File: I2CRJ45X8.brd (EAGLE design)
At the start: 80 x 50 mm, 59 parts, among them IC1 MCP23017SO, IC2 MCP23017SO, J1 M02X3-SHROUDED, J2 INT2A, J3 M02X3-PIN, J4 M02X3-PIN, J5 RJ45-X8, J6 M02X3-SHROUDED, J7 INT1A

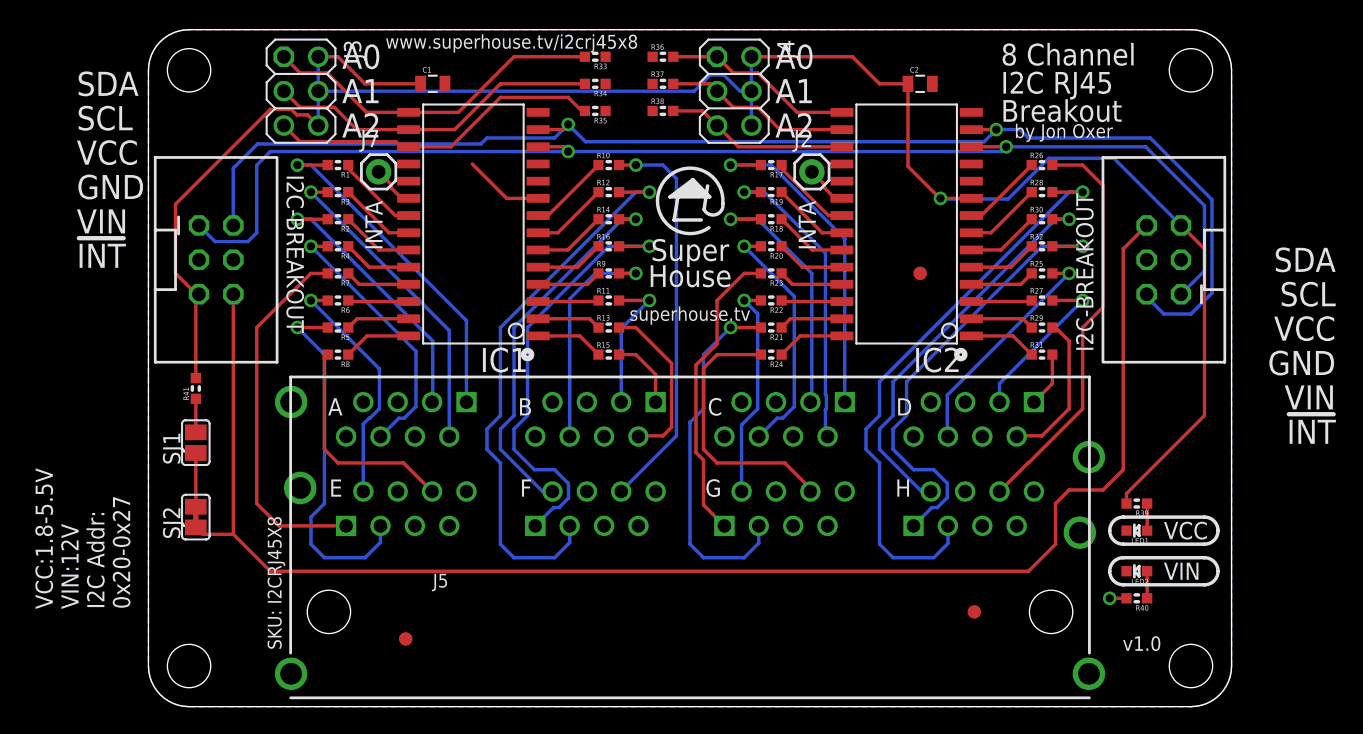
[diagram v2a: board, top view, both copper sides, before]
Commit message: Routing for 2x3 I2C Breakout header
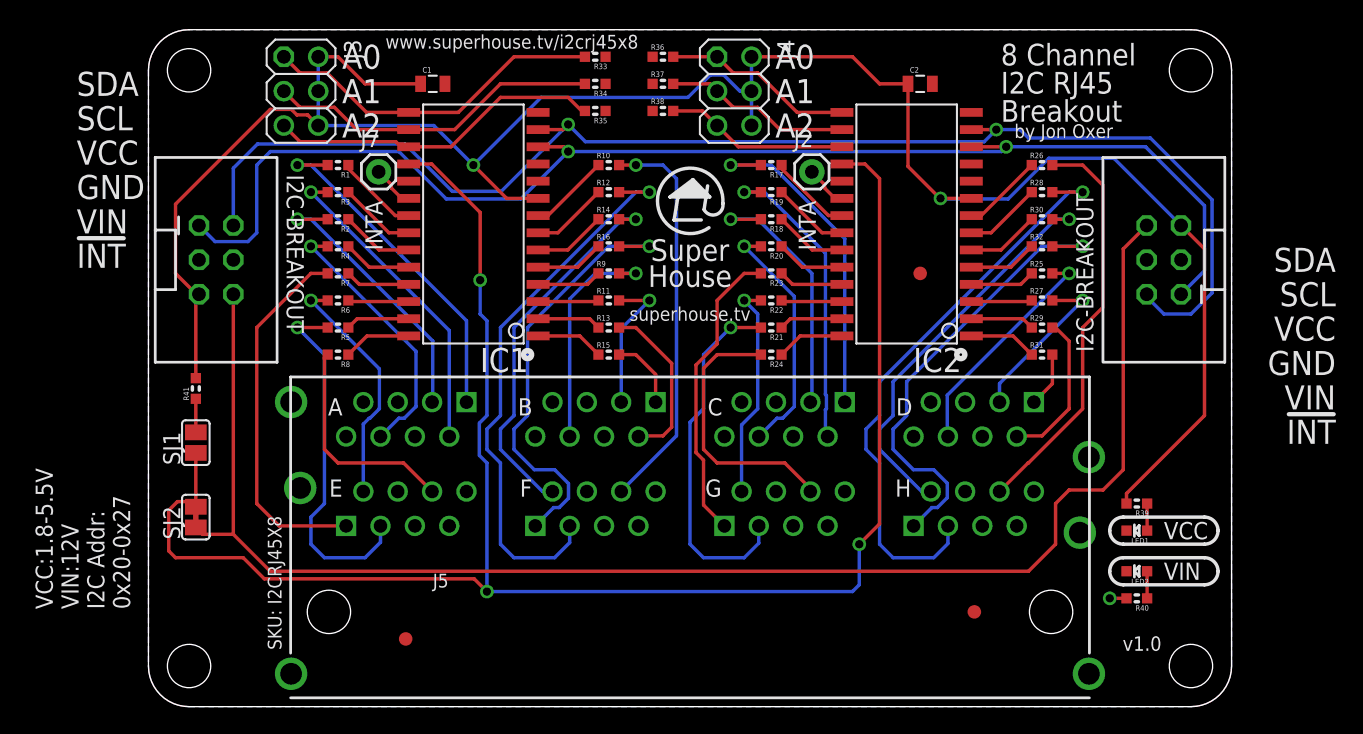
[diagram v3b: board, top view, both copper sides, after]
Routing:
- net !RST: track 3.98 -> 131.0 mm, vias 0 -> 3
- net VCC: track 154.3 -> 157.7 mm, vias 1 -> 2
- net SDA: track 98.2 -> 101.1 mm
- net SCL: track 94.6 -> 97.5 mm
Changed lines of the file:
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@@
 <wire x1="77" y1="29" x2="78.5588" y2="30.5588" width="0.254" layer="16"/>
 <wire x1="78.5588" y1="30.5588" x2="78.5588" y2="37.4412" width="0.254" layer="16"/>
-<wire x1="31" y1="43" x2="30" y2="42" width="0.254" layer="16"/>
-<wire x1="30" y1="42" x2="25" y2="42" width="0.254" layer="16"/>
-<wire x1="25" y1="42" x2="24.5588" y2="41.5588" width="0.254" layer="16"/>
 <wire x1="6.27" y1="39.77" x2="6.27" y2="35.54" width="0.254" layer="16"/>
-<wire x1="24.5588" y1="41.5588" x2="8.0588" y2="41.5588" width="0.254" layer="16"/>
-<wire x1="8.0588" y1="41.5588" x2="6.27" y2="39.77" width="0.254" layer="16"/>
+<wire x1="6.27" y1="39.77" x2="8.0588" y2="41.5588" width="0.254" layer="16"/>
+<wire x1="8.0588" y1="41.5588" x2="18.9412" y2="41.5588" width="0.254" layer="16"/>
+<wire x1="18.9412" y1="41.5588" x2="22.4412" y2="38.0588" width="0.254" layer="16"/>
+<wire x1="22.4412" y1="38.0588" x2="26.0588" y2="38.0588" width="0.254" layer="16"/>
+<wire x1="26.0588" y1="38.0588" x2="31" y2="43" width="0.254" layer="16"/>
 </signal>
 <signal name="SCL">
@@
 <wire x1="78" y1="32.19" x2="76.27" y2="30.46" width="0.254" layer="16"/>
 <wire x1="9" y1="41" x2="8" y2="40" width="0.254" layer="16"/>
-<wire x1="31" y1="41" x2="9" y2="41" width="0.254" layer="16"/>
 <wire x1="7.3462" y1="34.3462" x2="4.9238" y2="34.3462" width="0.254" layer="16"/>
 <wire x1="4.9238" y1="34.3462" x2="3.73" y2="35.54" width="0.254" layer="16"/>
 <wire x1="8" y1="40" x2="8" y2="35" width="0.254" layer="16"/>
 <wire x1="8" y1="35" x2="7.3462" y2="34.3462" width="0.254" layer="16"/>
+<wire x1="31" y1="41" x2="27.5" y2="37.5" width="0.254" layer="16"/>
+<wire x1="22" y1="37.5" x2="19.5" y2="40" width="0.254" layer="16"/>
+<wire x1="19.5" y1="40" x2="18.5" y2="41" width="0.254" layer="16"/>
+<wire x1="18.5" y1="41" x2="9" y2="41" width="0.254" layer="16"/>
+<wire x1="27.5" y1="37.5" x2="22" y2="37.5" width="0.254" layer="16"/>
 </signal>
 <signal name="E1">
@@
 <wire x1="58.5" y1="37.54" x2="60.78" y2="37.54" width="0.254" layer="1"/>
 <contactref element="C1" pad="1"/>
-<wire x1="23.92" y1="40.08" x2="26.46" y2="37.54" width="0.254" layer="1"/>
+<wire x1="26.46" y1="37.54" x2="24" y2="40" width="0.254" layer="1"/>
 <contactref element="C2" pad="1"/>
 <contactref element="J4" pad="6"/>
@@
 <wire x1="16" y1="46" x2="14" y2="48" width="0.254" layer="1"/>
 <wire x1="44" y1="45.46" x2="44.54" y2="46" width="0.254" layer="16"/>
-<wire x1="41.50550625" y1="46.6538" x2="42.49449375" y2="46.6538" width="0.254" layer="16"/>
-<wire x1="12.54" y1="45.46" x2="40.31170625" y2="45.46" width="0.254" layer="16"/>
+<wire x1="42.49449375" y1="46.6538" x2="41.50550625" y2="46.6538" width="0.254" layer="16"/>
 <wire x1="43.68829375" y1="45.46" x2="44" y2="45.46" width="0.254" layer="16"/>
-<wire x1="40.31170625" y1="45.46" x2="41.50550625" y2="46.6538" width="0.254" layer="16"/>
 <wire x1="42.49449375" y1="46.6538" x2="43.68829375" y2="45.46" width="0.254" layer="16"/>
 <wire x1="10.96233125" y1="43.7074" x2="11.7526" y2="43.7074" width="0.254" layer="1"/>
@@
 <wire x1="3.5" y1="24.262" x2="3.5" y2="30.23" width="0.254" layer="1"/>
 <wire x1="3.5" y1="30.23" x2="3.73" y2="30.46" width="0.254" layer="1"/>
-<wire x1="20.1" y1="46" x2="23.92" y2="40.08" width="0" layer="19" extent="1-1"/>
+<wire x1="23.92" y1="40.08" x2="24" y2="40" width="0.254" layer="1"/>
+<via x="24" y="40" extent="1-16" drill="0.6096"/>
+<wire x1="12.54" y1="42.92" x2="21.08" y2="42.92" width="0.254" layer="16"/>
+<wire x1="21.08" y1="42.92" x2="24" y2="40" width="0.254" layer="16"/>
+<wire x1="29" y1="45" x2="24" y2="40" width="0.254" layer="16"/>
+<wire x1="41.50550625" y1="46.6538" x2="39.85170625" y2="45" width="0.254" layer="16"/>
+<wire x1="39.85170625" y1="45" x2="29" y2="45" width="0.254" layer="16"/>
 </signal>
 <signal name="N$2">
@@
 <contactref element="IC1" pad="18"/>
 <contactref element="IC2" pad="18"/>
-<wire x1="3.5" y1="18.738" x2="3.5" y2="14.762" width="0.254" layer="1"/>
-<wire x1="19.22" y1="40.08" x2="51.22" y2="40.08" width="0" layer="19" extent="1-1"/>
-<wire x1="3.5" y1="18.738" x2="19.22" y2="40.08" width="0" layer="19" extent="1-1"/>
+<wire x1="3.5" y1="18.738" x2="3.5" y2="15.143" width="0.254" layer="1"/>
+<wire x1="3.5" y1="15.143" x2="3.5" y2="14.762" width="0.254" layer="1"/>
+<wire x1="19.22" y1="40.08" x2="20.92" y2="40.08" width="0.254" layer="1"/>
+<wire x1="24.5" y1="36.5" x2="24.5" y2="31.5" width="0.254" layer="1"/>
+<via x="24.5" y="31.5" extent="1-16" drill="0.6096"/>
+<wire x1="24.5" y1="29" x2="25" y2="28.5" width="0.254" layer="16"/>
+<wire x1="25" y1="28.5" x2="25" y2="21.5" width="0.254" layer="16"/>
+<wire x1="24.4412" y1="18.5588" x2="25" y2="18" width="0.254" layer="16"/>
+<via x="25" y="8.5" extent="1-16" drill="0.6096"/>
+<wire x1="25" y1="8.5" x2="24.0588" y2="9.4412" width="0.254" layer="1"/>
+<wire x1="2" y1="11" x2="1.5" y2="11.5" width="0.254" layer="1"/>
+<wire x1="1.5" y1="11.5" x2="1.5" y2="14.5" width="0.254" layer="1"/>
+<wire x1="1.5" y1="14.5" x2="2.143" y2="15.143" width="0.254" layer="1"/>
+<wire x1="2.143" y1="15.143" x2="3.5" y2="15.143" width="0.254" layer="1"/>
+<wire x1="20.92" y1="40.08" x2="24.5" y2="36.5" width="0.254" layer="1"/>
+<wire x1="24.5" y1="31.5" x2="24.5" y2="29" width="0.254" layer="16"/>
+<wire x1="25" y1="21.5" x2="24.4412" y2="20.9412" width="0.254" layer="16"/>
+<wire x1="24.4412" y1="20.9412" x2="24.4412" y2="18.5588" width="0.254" layer="16"/>
+<wire x1="25" y1="18" x2="25" y2="8.5" width="0.254" layer="16"/>
+<wire x1="24.0588" y1="9.4412" x2="8.5588" y2="9.4412" width="0.254" layer="1"/>
+<wire x1="8.5588" y1="9.4412" x2="7" y2="11" width="0.254" layer="1"/>
+<wire x1="7" y1="11" x2="2" y2="11" width="0.254" layer="1"/>
+<wire x1="51.22" y1="40.08" x2="52.92" y2="40.08" width="0.254" layer="1"/>
+<wire x1="52.92" y1="40.08" x2="54" y2="39" width="0.254" layer="1"/>
+<wire x1="54" y1="39" x2="54" y2="13.5" width="0.254" layer="1"/>
+<via x="52.5" y="12" extent="1-16" drill="0.6096"/>
+<wire x1="52.5" y1="12" x2="52.5" y2="9" width="0.254" layer="16"/>
+<wire x1="52.5" y1="9" x2="52" y2="8.5" width="0.254" layer="16"/>
+<wire x1="52" y1="8.5" x2="25" y2="8.5" width="0.254" layer="16"/>
+<wire x1="54" y1="13.5" x2="52.5" y2="12" width="0.254" layer="1"/>
 </signal>
 <signal name="N$14">

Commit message: Converted to I2C-BREAKOUT header for v2.0 release
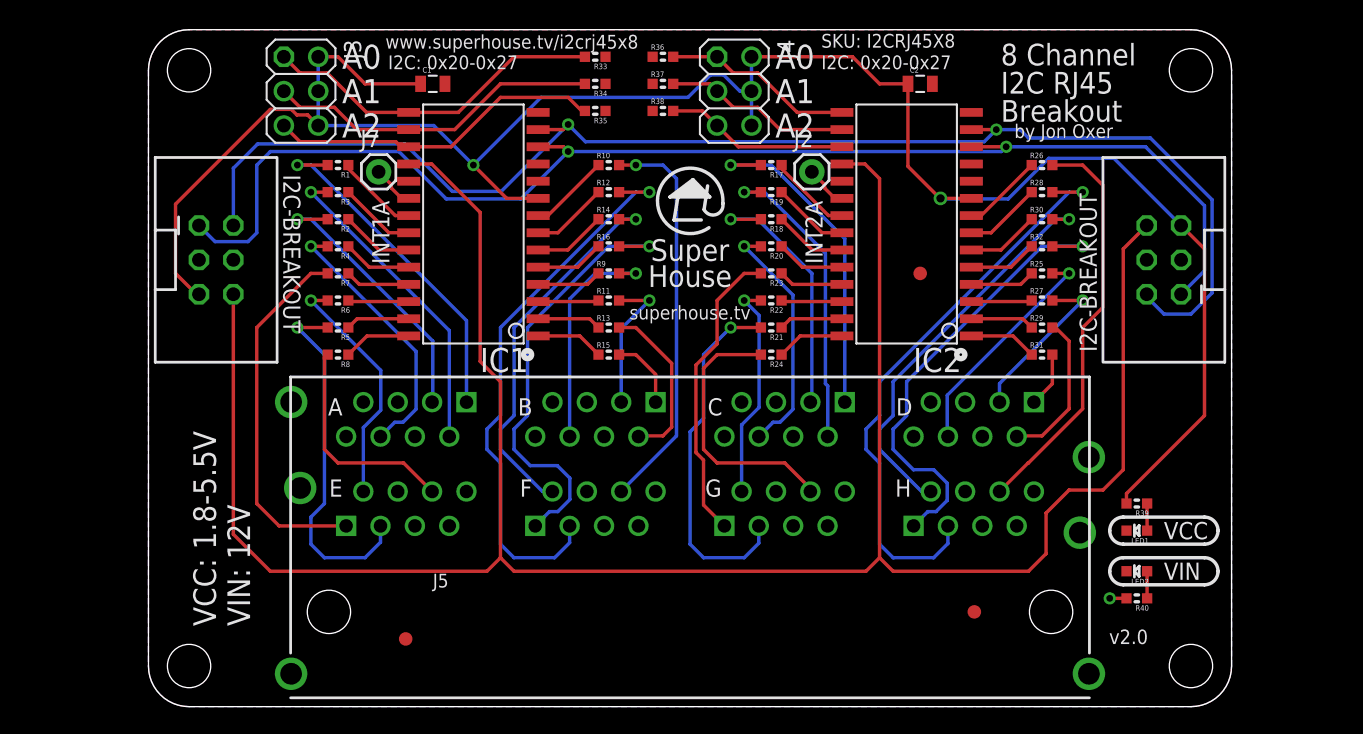
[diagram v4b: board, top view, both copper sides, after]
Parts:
- removed R41: 10K, SuperHouse-DiscreteSemi:R0603
- removed SJ1: (no value), SuperHouse-Jumpers:SJ
- removed SJ2: SJC-NORMAL, SuperHouse-Jumpers:SJC
- J1, J6: value M02X3-SHROUDED -> I2C-BREAKOUT
- R40: value 10K -> 1K
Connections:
- removed net !RST: IC1.18, IC2.18, SJ1.1, SJ2.2
- removed net N$14: R41.1, SJ1.2
- net !RESET: now also IC1.18, IC2.18; no longer SJ2.1
- net VCC: no longer R41.2
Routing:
- net !RST: track 131.0 -> 0.00 mm, vias 3 -> 0
- net !RESET: track 111.2 -> 174.0 mm
- net VCC: track 157.7 -> 151.1 mm
- net N$14: track 2.48 -> 0.00 mm
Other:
- board text added: "!RST"
- board text added: "(C)2019-2020 SuperHouse Automation Pty Ltd Released under the terms of the TAPR Open Hardware License: www.tapr.org/OHL"
- board text added: "I2C: 0x20-0x27"
- board text added: "INT1A"
- board text added: "INT2A"
- board text added: "VCC: 1.8-5.5V VIN: 12V"
- board text added: "v2.0"
- board text removed: "!INT"
- board text removed: "(C)2019 SuperHouse Automation Pty Ltd Released under the terms of the TAPR Open Hardware License: www.tapr.org/OHL"
- board text removed: "INTA"
- board text removed: "VCC:1.8-5.5V VIN:12V I2C Addr: 0x20-0x27"
- board text removed: "v1.0"
